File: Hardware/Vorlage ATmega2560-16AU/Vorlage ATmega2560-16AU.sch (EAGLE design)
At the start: 118 parts, among them IC1 CD74HC14PW, IC2 ATMEGA2560640V-8AU, IC3 SS39E, IC4 SS39E, IC5 74AC138D, IC6 XC6210B332MR, Q1 16MHz, Q10 PMV27UPER, Q2 32.768kHz, Q3 PMV27UPER, Q4 PMV27UPER, Q5 PMV27UPER, Q6 PMV27UPER, Q7 PMV27UPER, Q8 PMV27UPER, Q9 PMV27UPER, U1 LM35DZ, X1 2510-, X2 +5V, X3 2514-, X4 2510-

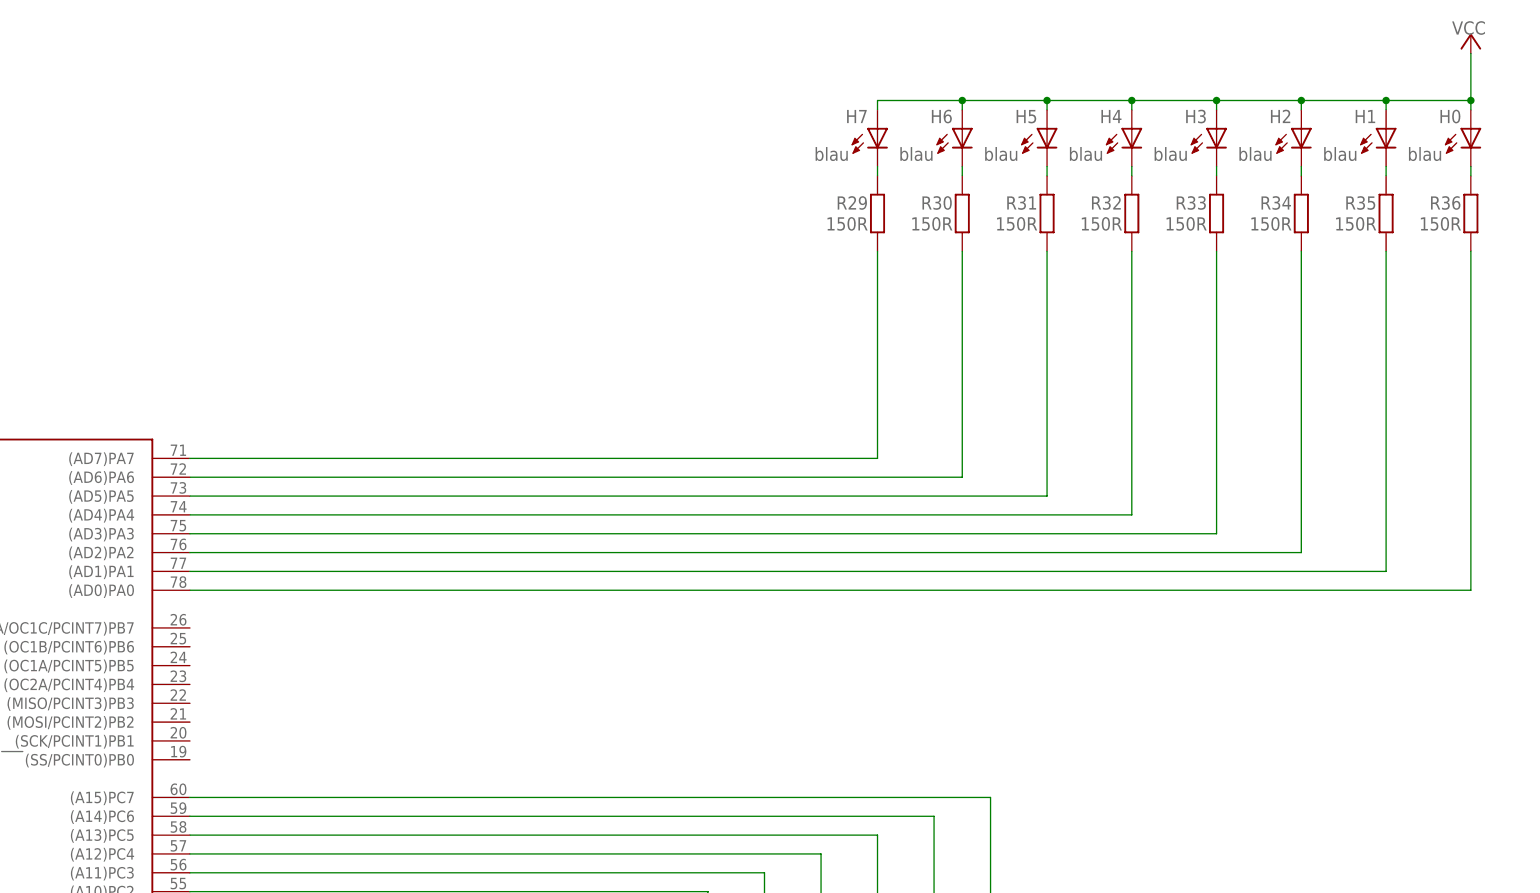
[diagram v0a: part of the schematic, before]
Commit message: LEDs neu über FET
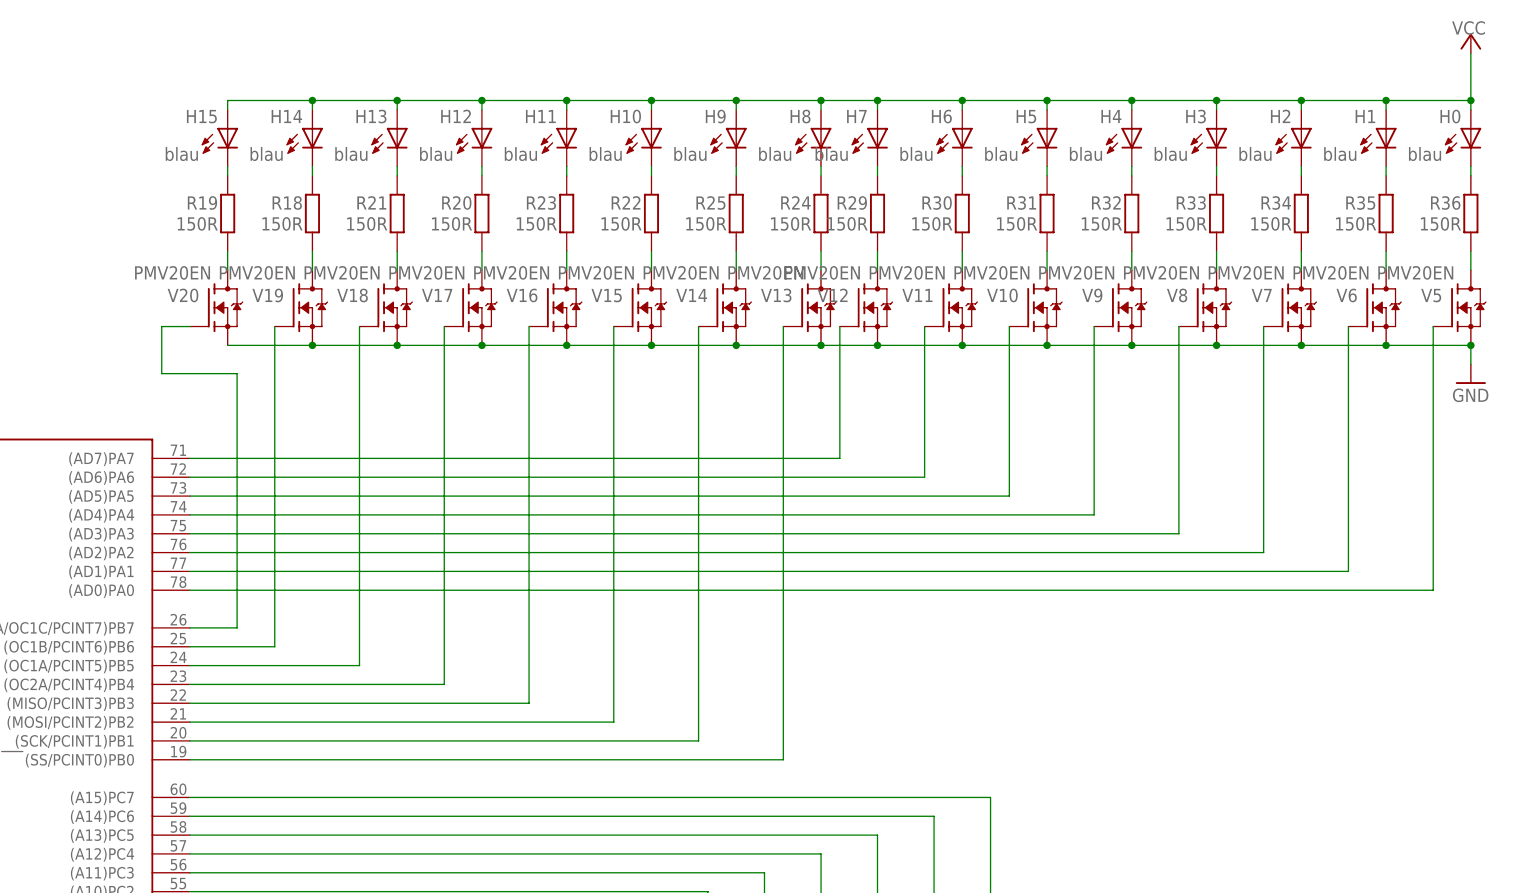
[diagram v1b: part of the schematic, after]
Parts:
- added H10, H11, H12, H13, H14, H15, H8, H9: blau, led:LEDCHIPLED_1206
- added R18, R19, R20, R21, R22, R23, R24, R25: 150R, rcl:R-EU_R1206
- added V10, V11, V12, V13, V14, V15, V16, V17, V18, V19, V20, V5, V6, V7, V8, V9: PMV20EN, transistor-fet-mit-BSS138:BSS138
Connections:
- new net H1: H15.C, R19.2
- new net N$13: R33.1, V8.D
- new net N$14: R32.1, V9.D
- new net N$15: R31.1, V10.D
- new net N$16: R30.1, V11.D
- new net N$17: R29.1, V12.D
- new net N$45: IC2.(AD0)PA0, V5.G
- new net N$46: H14.C, R18.2
- new net N$47: H12.C, R20.2
- new net N$51: H13.C, R21.2
- new net N$52: H10.C, R22.2
- new net N$55: H11.C, R23.2
- new net N$56: H8.C, R24.2
- new net N$59: H9.C, R25.2
- new net N$61: R24.1, V13.D
- new net N$63: R25.1, V14.D
- new net N$69: R19.1, V20.D
- new net N$71: IC2.(AD1)PA1, V6.G
- new net N$72: IC2.(AD2)PA2, V7.G
- new net N$74: IC2.(AD3)PA3, V8.G
- new net N$76: IC2.(AD4)PA4, V9.G
- new net N$77: IC2.(AD5)PA5, V10.G
- new net N$78: IC2.(AD6)PA6, V11.G
- new net N$79: IC2.(AD7)PA7, V12.G
- new net N$80: IC2.(SS/PCINT0)PB0, V13.G
- new net N$81: IC2.(SCK/PCINT1)PB1, V14.G
- new net N$82: IC2.(MOSI/PCINT2)PB2, V15.G
- new net N$83: IC2.(MISO/PCINT3)PB3, V16.G
- new net N$84: IC2.(OC2A/PCINT4)PB4, V17.G
- new net N$85: IC2.(OC1A/PCINT5)PB5, V18.G
- new net N$86: IC2.(OC1B/PCINT6)PB6, V19.G
- new net N$87: IC2.(OC0A/OC1C/PCINT7)PB7, V20.G
- net GND: now also V10.S, V11.S, V12.S, V13.S, V14.S, V15.S, V16.S, V17.S, V18.S, V19.S, V20.S, V5.S, V6.S, V7.S, V8.S, V9.S
- net N$5: now also R36.1, V5.D; no longer IC2.(AD7)PA7, R29.1
- net N$6: now also R35.1, V6.D; no longer IC2.(AD6)PA6, R30.1
- net N$64: now also R22.1, V15.D; no longer IC2.(AD0)PA0, R36.1
- net N$65: now also R23.1, V16.D; no longer IC2.(AD1)PA1, R35.1
- net N$66: now also R20.1, V17.D; no longer IC2.(AD2)PA2, R34.1
- net N$67: now also R21.1, V18.D; no longer IC2.(AD3)PA3, R33.1
- net N$68: now also R18.1, V19.D; no longer IC2.(AD4)PA4, R32.1
- net N$7: now also R34.1, V7.D; no longer IC2.(AD5)PA5, R31.1
- net VCC: now also H10.A, H11.A, H12.A, H13.A, H14.A, H15.A, H8.A, H9.A

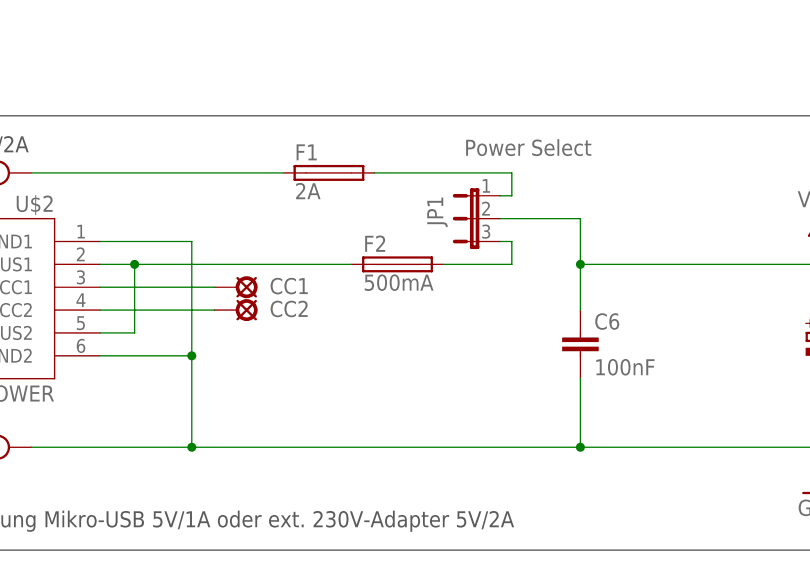
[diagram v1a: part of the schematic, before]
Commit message: Sicherung F1 ist 2A
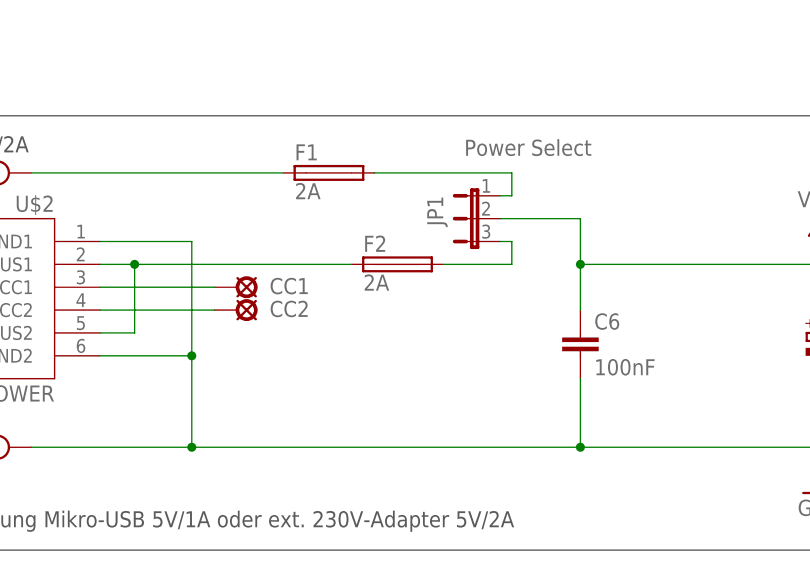
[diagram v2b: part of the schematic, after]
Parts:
- F2: value 500mA -> 2A
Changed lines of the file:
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@@
 <part name="C20" library="rcl" library_urn="urn:adsk.eagle:library:334" deviceset="C-EU" device="C1206" package3d_urn="urn:adsk.eagle:package:23618/2" value="1uF"/>
 <part name="C21" library="rcl" library_urn="urn:adsk.eagle:library:334" deviceset="C-EU" device="C1206" package3d_urn="urn:adsk.eagle:package:23618/2" value="100nF"/>
-<part name="F2" library="fuse" deviceset="19560" device="1206" value="500mA"/>
+<part name="F2" library="fuse" deviceset="19560" device="1206" value="2A"/>
 <part name="C6" library="rcl" library_urn="urn:adsk.eagle:library:334" deviceset="C-EU" device="C1206" package3d_urn="urn:adsk.eagle:package:23618/2" value="100nF"/>
 <part name="P+2" library="supply1" library_urn="urn:adsk.eagle:library:371" deviceset="VCC" device=""/>
